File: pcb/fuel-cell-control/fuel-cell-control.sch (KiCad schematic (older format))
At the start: 1 part

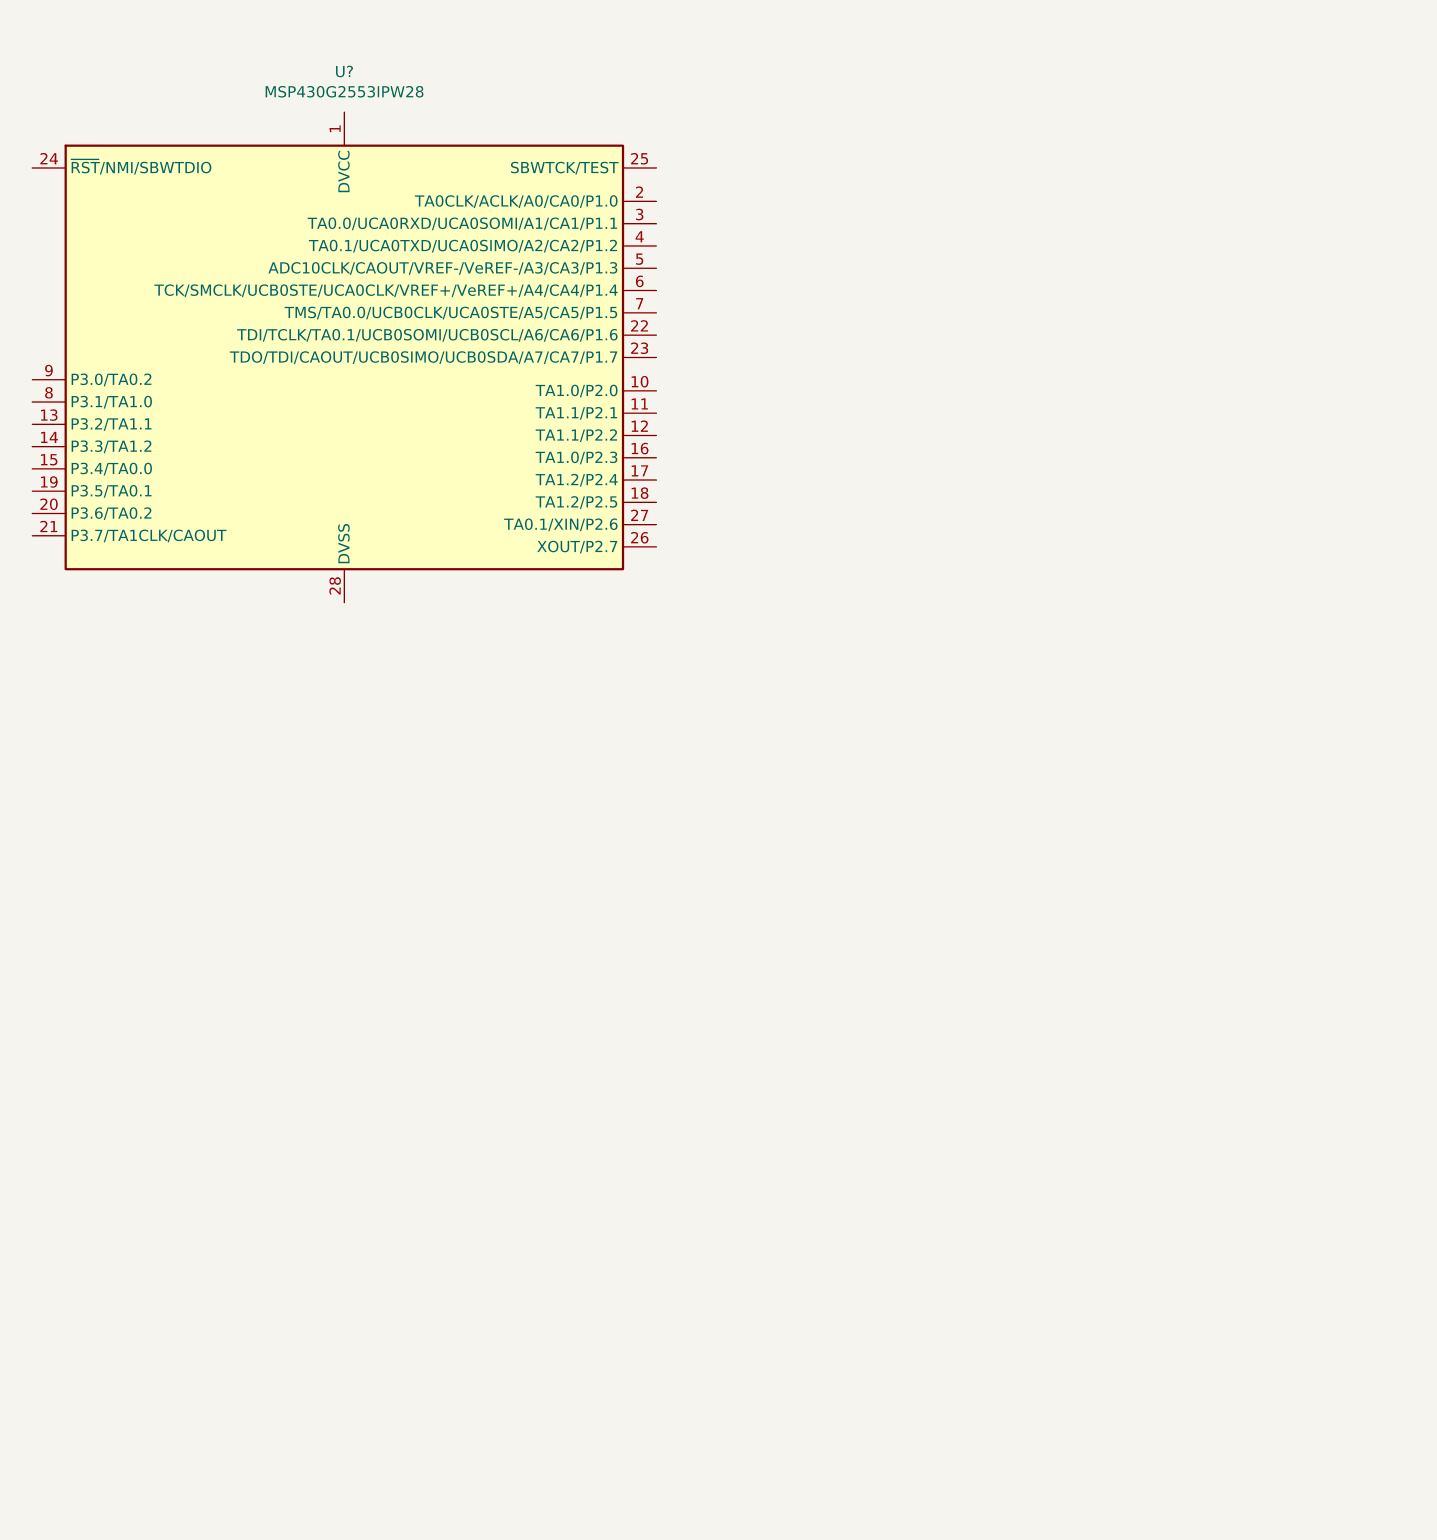
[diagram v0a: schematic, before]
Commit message: Adds MUXes, DCDC Converter, and relevant libraries
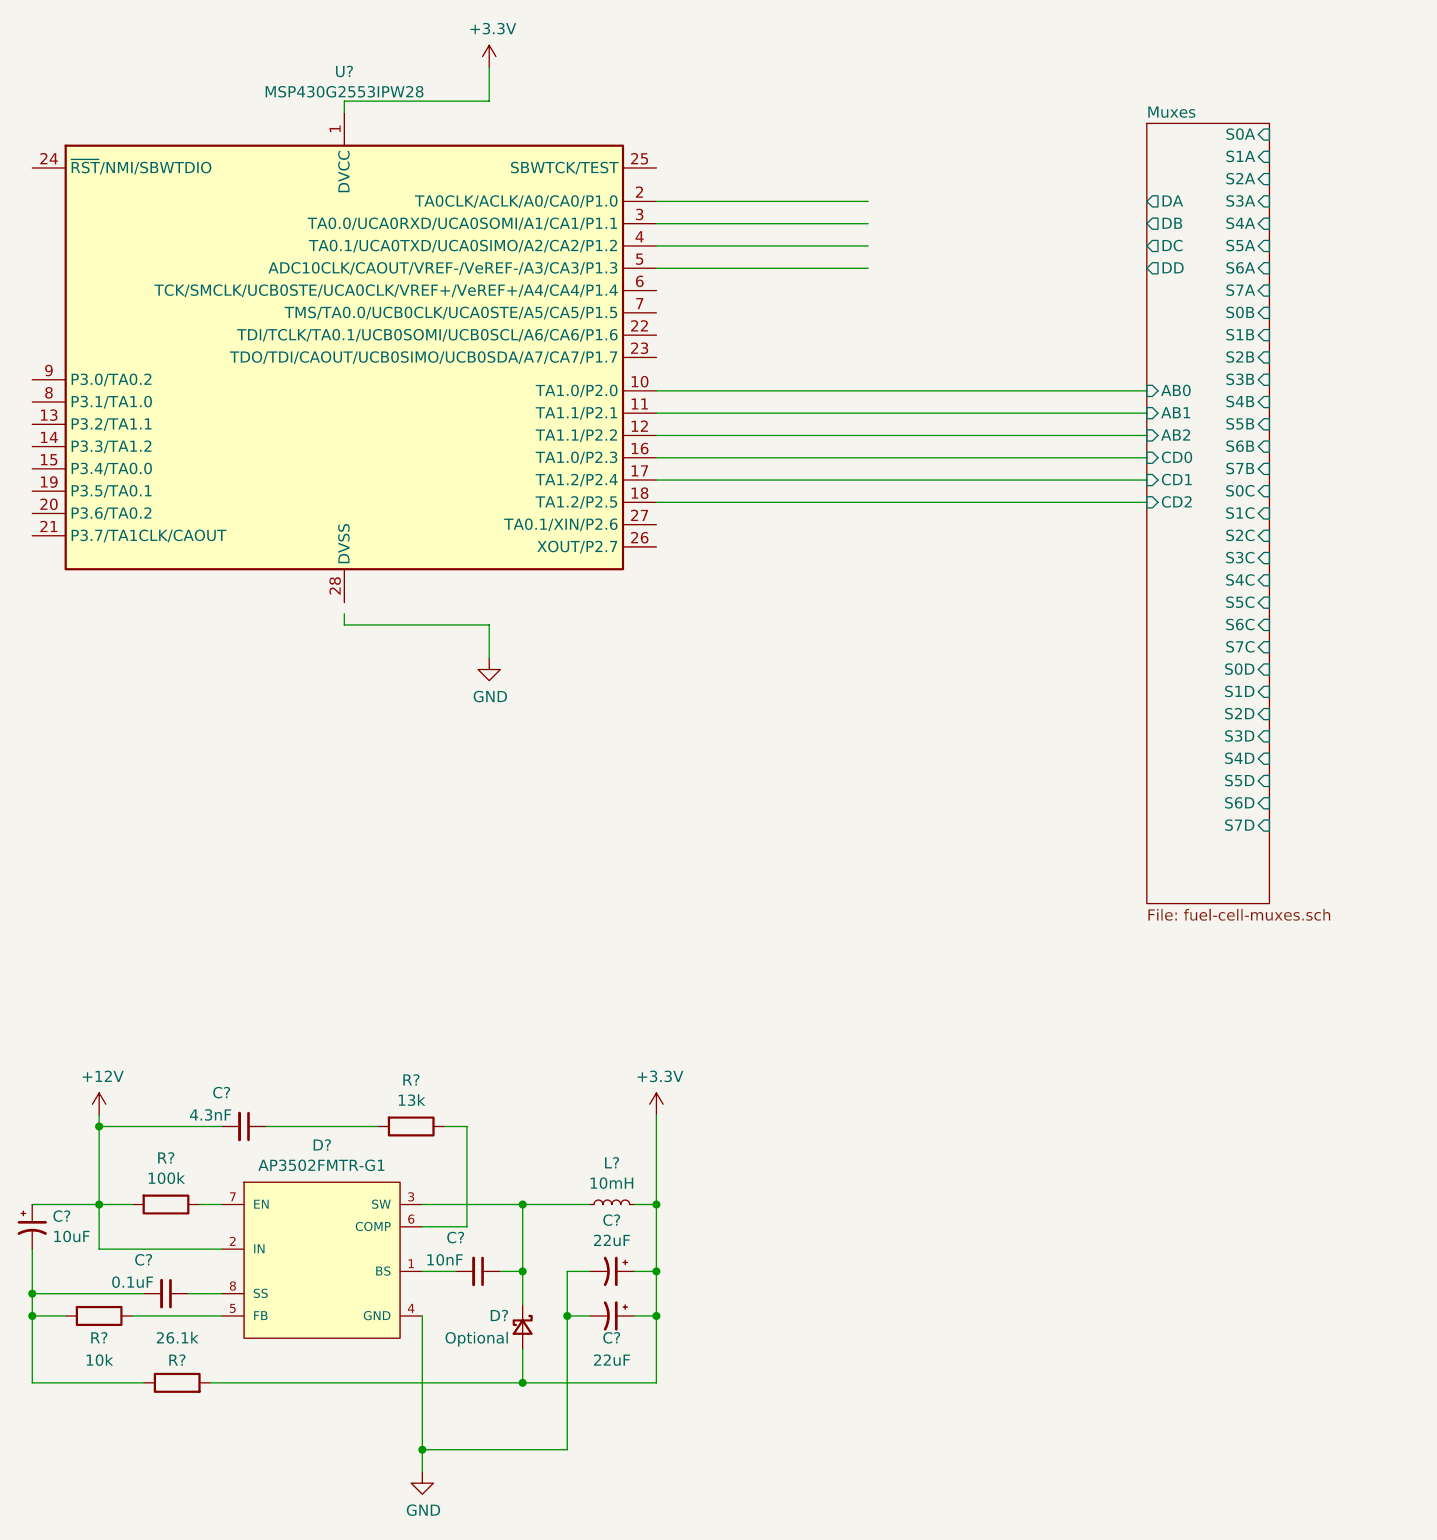
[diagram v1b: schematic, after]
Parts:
- added C?: 10uF, symbol Device:CP1_Small
- added C?: 0.1uF, symbol Device:C_Small
- added C? (x2): 22uF, symbol Device:CP1_Small
- added C?: 10nF, symbol Device:C_Small
- added C?: 4.3nF, symbol Device:C_Small
- added D?: AP3502FMTR-G1, Diodes-AP3502FMTR-G1-March_2017-2017-03-14-*, symbol eec:AP3502FMTR-G1
- added D?: Optional, symbol Device:D_Schottky_Small
- added L?: 10mH, symbol Device:L_Small
- added R?: 100k, symbol Device:R
- added R?: 10k, symbol Device:R
- added R?: 26.1k, symbol Device:R
- added R?: 13k, symbol Device:R
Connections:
- net labels added: +12V, +3.3V, GND
- wire segments 0 -> 59
